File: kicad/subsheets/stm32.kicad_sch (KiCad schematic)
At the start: 15 parts, among them J1 SWD, SW2 RESET, SW3 USER, U3 STM32U575RGT6

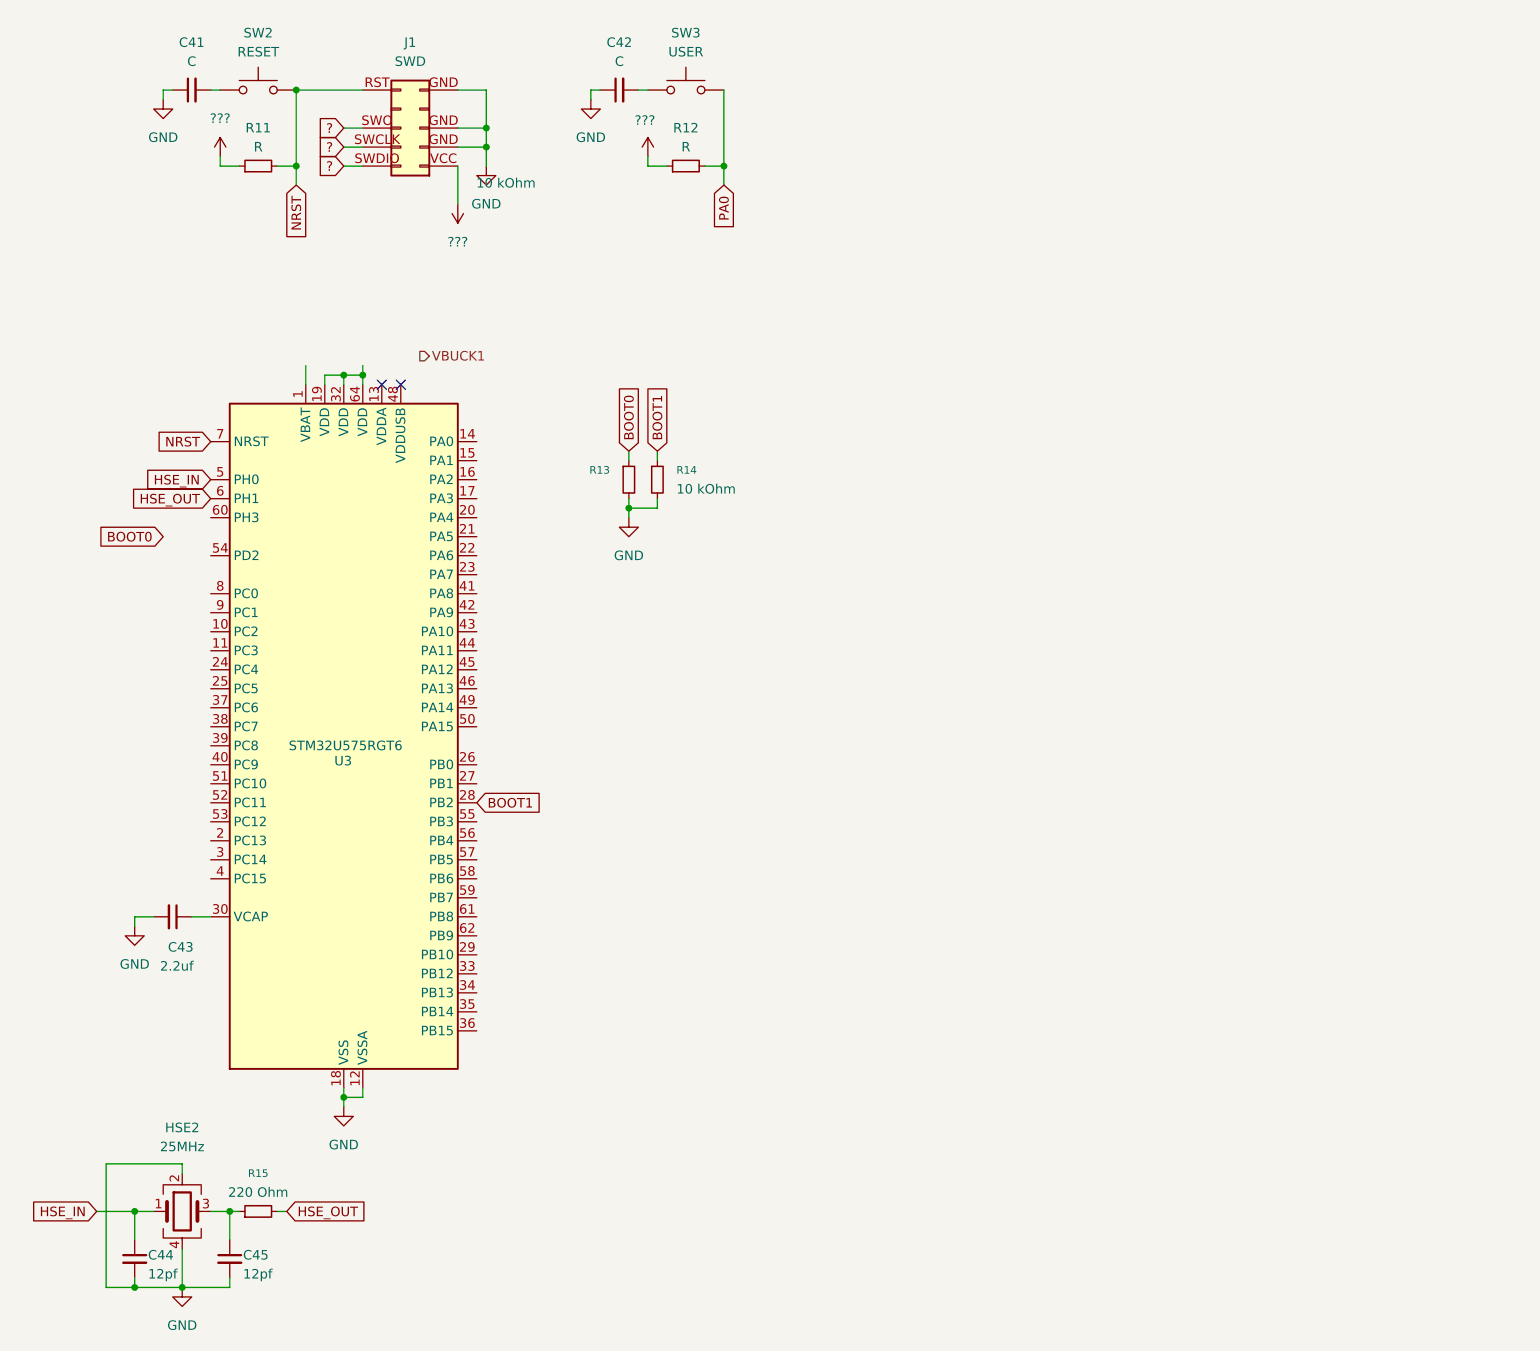
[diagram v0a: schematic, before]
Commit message: Wire peripherals to STM
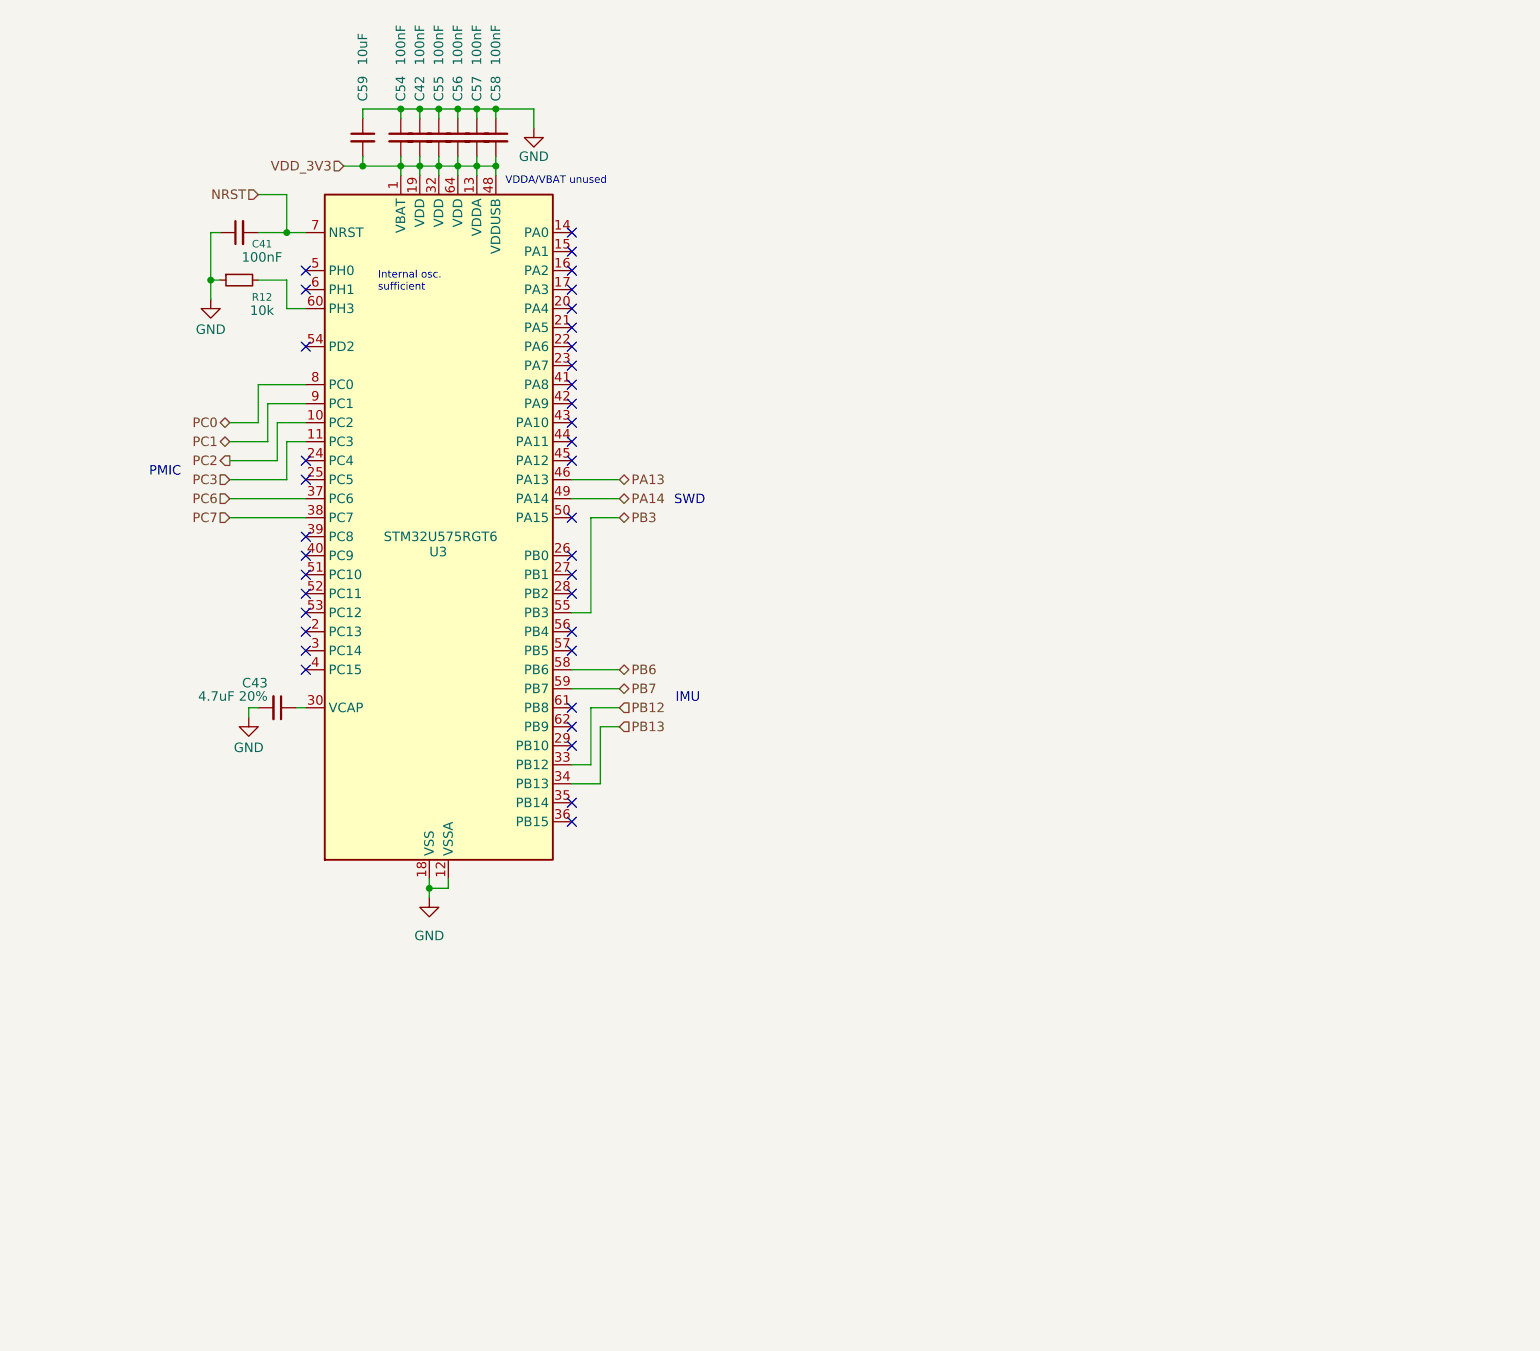
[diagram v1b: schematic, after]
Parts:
- removed C44, C45: 12pf, symbol Device:C_Small
- removed HSE2: 25MHz, symbol Device:Crystal_GND24
- removed J1: SWD, symbol Connector_Generic:Conn_02x05_Odd_Even
- removed R11: R, symbol Device:R_Small
- removed R13, R14: 10 kOhm, symbol Device:R_Small
- removed R15: 220 Ohm, symbol Device:R_Small
- removed SW2: RESET, symbol Switch:SW_Push
- removed SW3: USER, symbol Switch:SW_Push
- added C54, C55, C56, C57, C58: 100nF, symbol Device:C_Small
- added C59: 10uF, symbol Device:C_Small
- C41, C42: value C -> 100nF
- C43: value 2.2uf -> 4.7uF 20%
- R12: value R -> 10k
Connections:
- net ??? is gone; now on net GND: R12.1
- net PA0 is gone; now on an unnamed net: R12.2
- net GND: now also C54.1, C55.1, C56.1, C57.1, C58.1, C59.1; no longer U3.31 (VSS), U3.47 (VSS), U3.63 (VSS)
- net NRST: now also C41.2
- net VDD_3V3: now reaches C42.2
- net VDD_3V3: now also U3.1 (VBAT), U3.13 (VDDA), U3.19 (VDD), U3.32 (VDD), U3.48 (VDDUSB), U3.64 (VDD), C54.2, C55.2, C56.2, C57.2, C58.2, C59.2
- net PC2: now reaches U3.10 (PC2)
- net PC3: now reaches U3.11 (PC3)
- net PB12: now reaches U3.33 (PB12)
- net PB13: now reaches U3.34 (PB13)
- net PC6: now reaches U3.37 (PC6)
- net PC7: now reaches U3.38 (PC7)
- net PA13: now reaches U3.46 (PA13)
- net PA14: now reaches U3.49 (PA14)
- net PB3: now reaches U3.55 (PB3)
- net PB6: now reaches U3.58 (PB6)
- net PB7: now reaches U3.59 (PB7)
- net PC0: now reaches U3.8 (PC0)
- net PC1: now reaches U3.9 (PC1)
- net BOOT1: no longer names the net of U3.28 (PB2)
- net HSE_IN: no longer names the net of U3.5 (PH0)
- net HSE_OUT: no longer names the net of U3.6 (PH1)
- new net: U3.31 (VSS), U3.47 (VSS), U3.63 (VSS)
- no-connect marks 2 -> 37
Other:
- note added: "IMU"
- note added: "Internal osc. sufficient"
- note added: "PMIC"
- note added: "SWD"
- note added: "VDDA/VBAT unused"
- moved on the sheet: C41, C43, U3

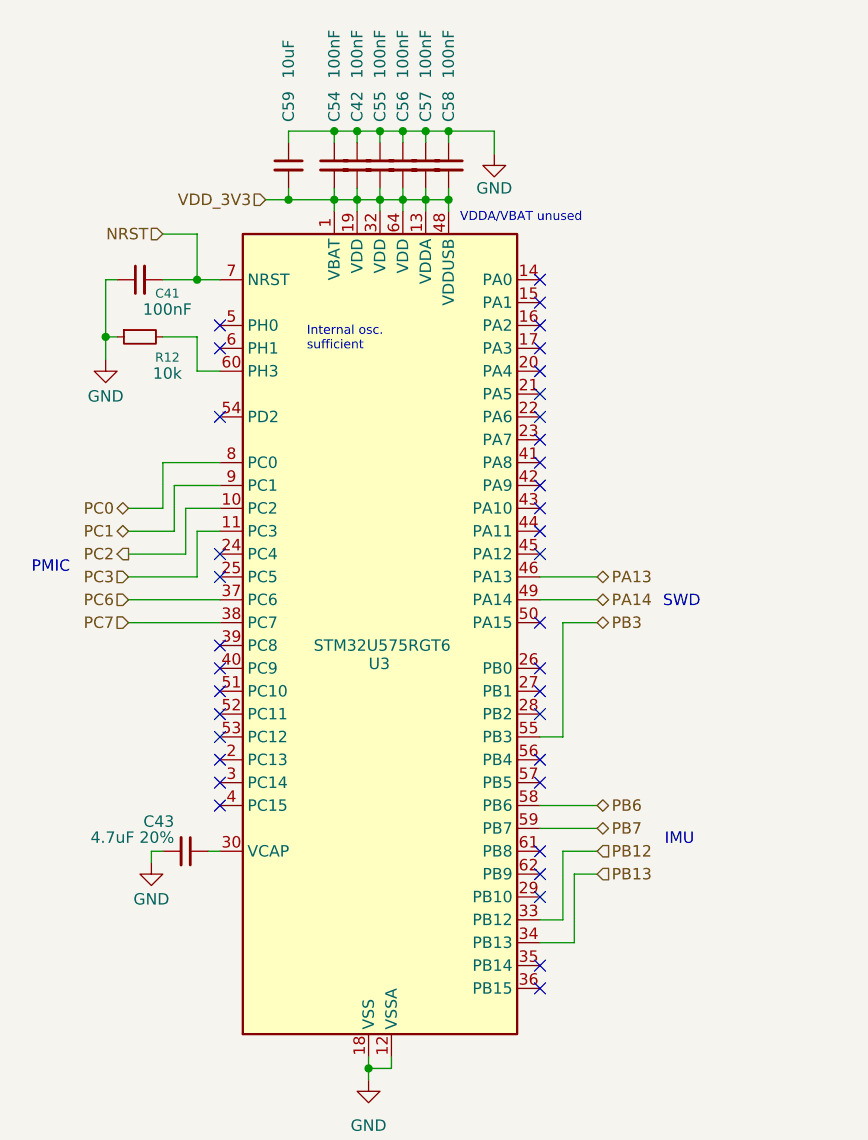
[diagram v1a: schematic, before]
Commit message: Wire microsd port
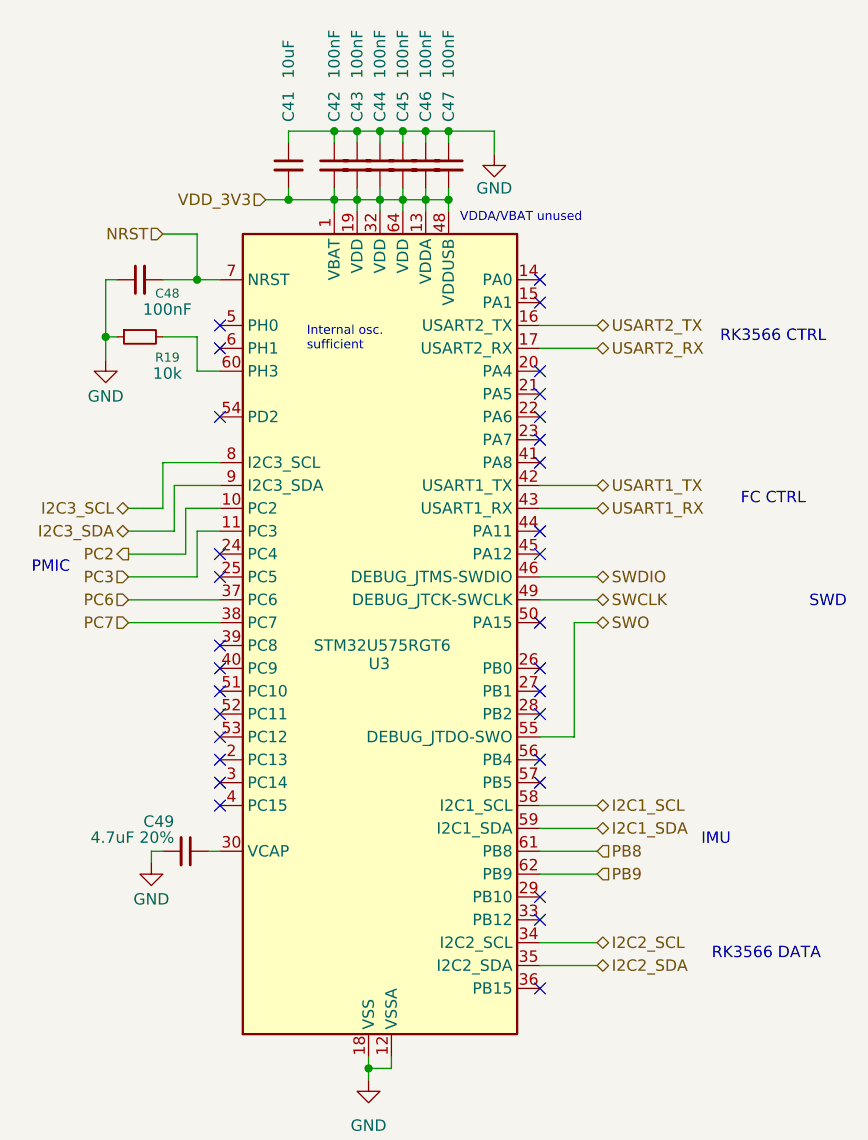
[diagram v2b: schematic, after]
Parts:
- renumbered C59 to C41, C54 to C42, C42 to C43, C55 to C44, C56 to C45, C57 to C46, C58 to C47, C41 to C48, C43 to C49, R12 to R19
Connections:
- net USART2_TX: now reaches U3.16 (PA2)
- net USART2_RX: now reaches U3.17 (PA3)
- net I2C2_SDA: now reaches U3.35 (PB14)
- net USART1_TX: now reaches U3.42 (PA9)
- net USART1_RX: now reaches U3.43 (PA10)
- net PB8: now reaches U3.61 (PB8)
- net PB9: now reaches U3.62 (PB9)
- net PA13 renamed SWDIO
- net PA14 renamed SWCLK
- net PB12: no longer names the net of U3.33 (PB12)
- net PB13 renamed I2C2_SCL
- net PB3 renamed SWO
- net PB6 renamed I2C1_SCL
- net PB7 renamed I2C1_SDA
- net PC0 renamed I2C3_SCL
- net PC1 renamed I2C3_SDA
- no-connect marks 37 -> 31
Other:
- note added: "FC CTRL"
- note added: "RK3566 CTRL"
- note added: "RK3566 DATA"

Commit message: Clean up root sheet, add power supply subsheet
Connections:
- net PA0: now reaches U3.14 (PA0)
- no-connect marks 31 -> 30
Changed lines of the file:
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@@
 	(text "SWD"
 		(exclude_from_sim no)
-		(at 119.634 81.534 0)
+		(at 104.902 81.534 0)
 		(effects
 			(font
@@
 	)
 	(no_connect
-		(at 87.63 45.72)
-	)
-	(no_connect
 		(at 52.07 53.34)
 	)
@@
 	(no_connect
 		(at 87.63 88.9)
+	)
+	(wire
+		(pts
+			(xy 93.98 45.72) (xy 87.63 45.72)
+		)
+		(stroke
+			(width 0)
+			(type default)
+		)
 	)
 	(wire
@@
 		(effects
 			(font
+				(size 1.27 1.27)
+			)
+			(justify left)
+		)
+	)
+	(hierarchical_label "PA0"
+		(shape output)
+		(at 93.98 45.72 0)
+		(effects
+			(font

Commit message: Make sure logic levels are correct between ICs
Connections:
- net I2C2_SCL: no longer names the net of U3.34 (PB13)
- net I2C2_SDA: no longer names the net of U3.35 (PB14)
- no-connect marks 30 -> 32
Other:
- note added: "RK3566 CTRL/DATA"
- note removed: "RK3566 CTRL"
- note removed: "RK3566 DATA"
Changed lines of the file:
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@@
 		)
 	)
-	(text "RK3566 CTRL"
+	(text "RK3566 \nCTRL/DATA"
 		(exclude_from_sim no)
-		(at 113.538 52.07 0)
-		(effects
-			(font
-				(size 1.27 1.27)
-			)
+		(at 107.188 52.324 0)
+		(effects
+			(font
+				(size 1.27 1.27)
+			)
+			(justify left)
 		)
 	)
@@
 		(exclude_from_sim no)
 		(at 104.902 81.534 0)
-		(effects
-			(font
-				(size 1.27 1.27)
-			)
-		)
-	)
-	(text "RK3566 DATA"
-		(exclude_from_sim no)
-		(at 112.776 120.65 0)
 		(effects
 			(font
@@
 	)
 	(no_connect
+		(at 87.63 119.38)
+	)
+	(no_connect
 		(at 87.63 76.2)
 	)
@@
 	)
 	(no_connect
+		(at 87.63 121.92)
+	)
+	(no_connect
 		(at 87.63 91.44)
 	)
@@
 	(wire
 		(pts
-			(xy 93.98 121.92) (xy 87.63 121.92)
-		)
-		(stroke
-			(width 0)
-			(type default)
-		)
-	)
-	(wire
-		(pts
 			(xy 41.91 78.74) (xy 49.53 78.74)
 		)
@@
 		(pts
 			(xy 64.77 29.21) (xy 67.31 29.21)
-		)
-		(stroke
-			(width 0)
-			(type default)
-		)
-	)
-	(wire
-		(pts
-			(xy 93.98 119.38) (xy 87.63 119.38)
 		)
 		(stroke
@@
 		(shape bidirectional)
 		(at 93.98 50.8 0)
-		(effects
-			(font
-				(size 1.27 1.27)
-			)
-			(justify left)
-		)
-	)
-	(hierarchical_label "I2C2_SDA"
-		(shape bidirectional)
-		(at 93.98 121.92 0)
-		(effects
-			(font
-				(size 1.27 1.27)
-			)
-			(justify left)
-		)
-	)
-	(hierarchical_label "I2C2_SCL"
-		(shape bidirectional)
-		(at 93.98 119.38 0)
 		(effects
 			(font
@@
 		)
 		(pin "34"
-			(alternate "I2C2_SCL")
 		)
 		(pin "29"
@@
 		)
 		(pin "35"
-			(alternate "I2C2_SDA")
 		)
 		(pin "3"
